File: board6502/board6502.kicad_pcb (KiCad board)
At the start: 2 copper layers, 48 parts, among them J1 IO Pinheader, J2 UART, J3 USB_B, J4 Expansion Port, J5 Power connector, SW1 Reset button, SW2 SW_NMI, U1 DS1813, U2 74LS00, U3 74LS04, U4 W65C22N, U5 74LS30, U6 W65C51N, U7 W65C02, U8 AT28C64B, U9 CY7C199, X1 1-10MHz, Y1 1.8432M

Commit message: start laying out components
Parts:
- J4: footprint Connector_PinHeader_2.54mm:PinHeader_2x17_P2.54mm_Horizontal -> Connector_PinHeader_2.54mm:PinHeader_2x17_P2.54mm_Vertical
- moved C11 277.8 mm to (324.0, 11.0)
- moved U8 239.0 mm to (299.0, 110.5), turned to 270 degrees
- moved J5 188.9 mm to (304.5, 39.0), turned to 90 degrees
- moved SW2 185.9 mm to (249.0, 32.0)
- moved X1 181.9 mm to (265.0, 42.5), turned to 270 degrees
- moved U7 179.1 mm to (260.0, 85.0), turned to 90 degrees
- moved C10 176.5 mm to (250.4, 163.3)
- moved C7 176.5 mm to (287.1, 166.8)
- moved C8 176.5 mm to (259.0, 163.3)
- moved R6 176.5 mm to (295.9, 167.7)
- moved R8 176.5 mm to (299.4, 163.7)
- moved R9 176.5 mm to (278.6, 168.0)
- moved C12 176.5 mm to (299.1, 159.1)
- moved J4 174.5 mm to (302.5, 32.0), turned to 270 degrees
- moved U9 161.7 mm to (293.5, 93.0), turned to 270 degrees
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
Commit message: complete layout
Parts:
- moved R9 124.8 mm to (296.5, 44.5)
- moved D4 121.1 mm to (301.5, 49.0), turned to 270 degrees
- moved R6 116.2 mm to (296.0, 51.5), turned to 90 degrees
- moved C12 114.7 mm to (302.5, 44.5)
- moved R8 112.4 mm to (307.0, 51.5), turned to 90 degrees
- moved C10 110.8 mm to (303.5, 66.0)
- moved C8 103.3 mm to (256.0, 60.0), turned to 270 degrees
- moved C11 94.1 mm to (256.5, 76.5), turned to 90 degrees
- moved C2 93.5 mm to (256.5, 92.5), turned to 270 degrees
- moved C7 53.8 mm to (256.5, 122.5), turned to 270 degrees
- moved R4 43.0 mm to (298.5, 39.5), turned to 180 degrees
- moved J4 42.1 mm to (260.5, 35.0), turned to 90 degrees
- moved C6 5.02 mm to (256.5, 116.5)
- moved C3 1.58 mm to (297.5, 93.0)
- moved U2 1.00 mm to (245.0, 72.0)
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
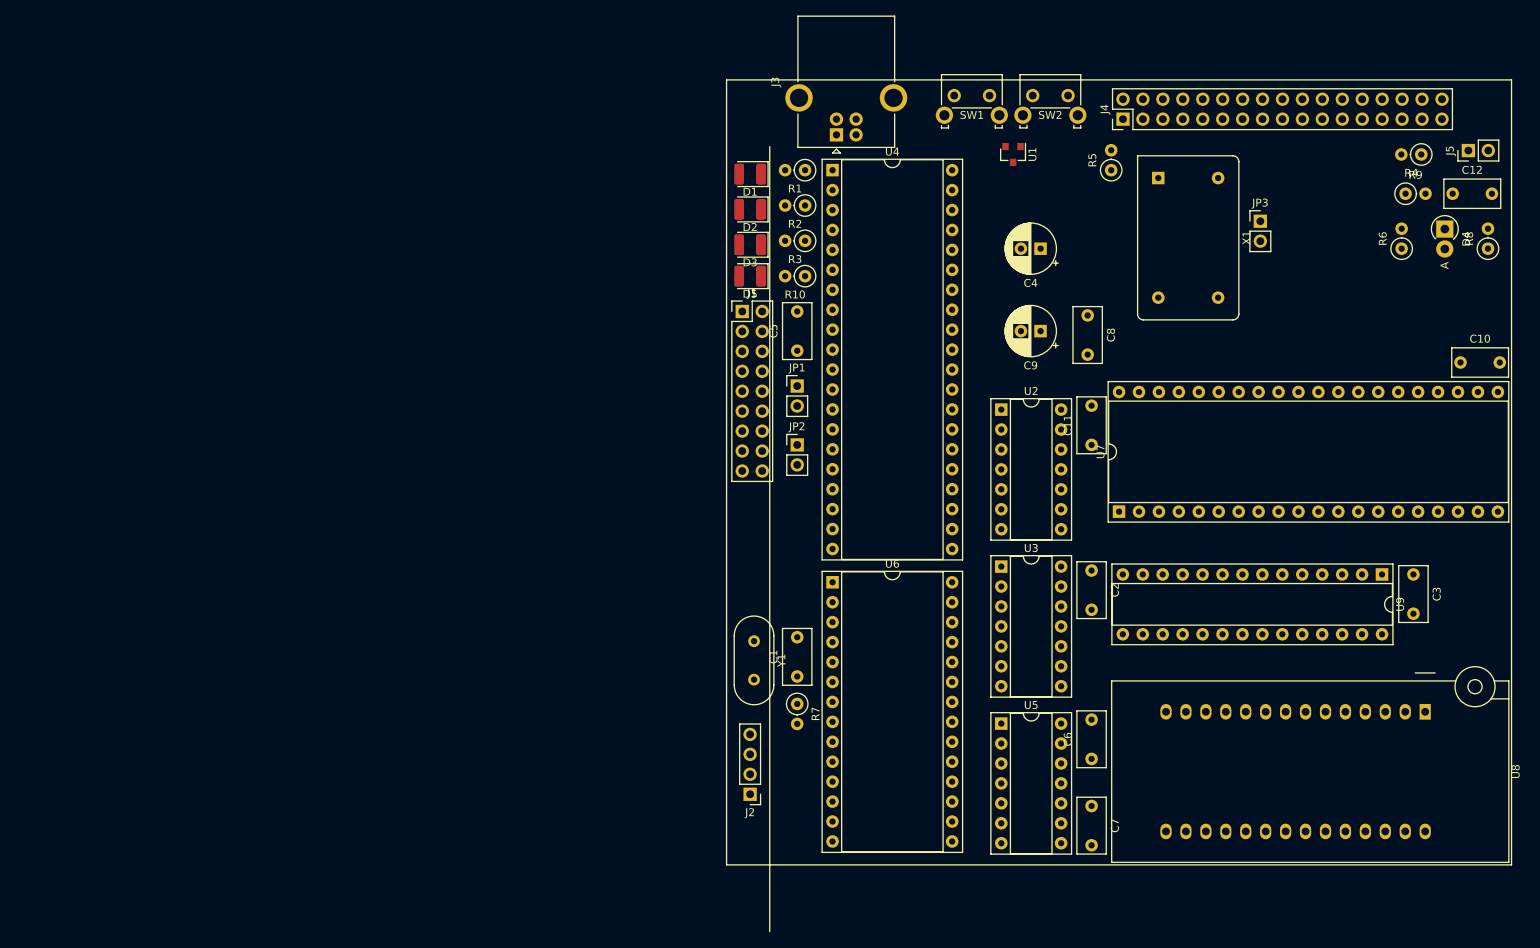
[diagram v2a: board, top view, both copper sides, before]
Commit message: update trace and via sizes
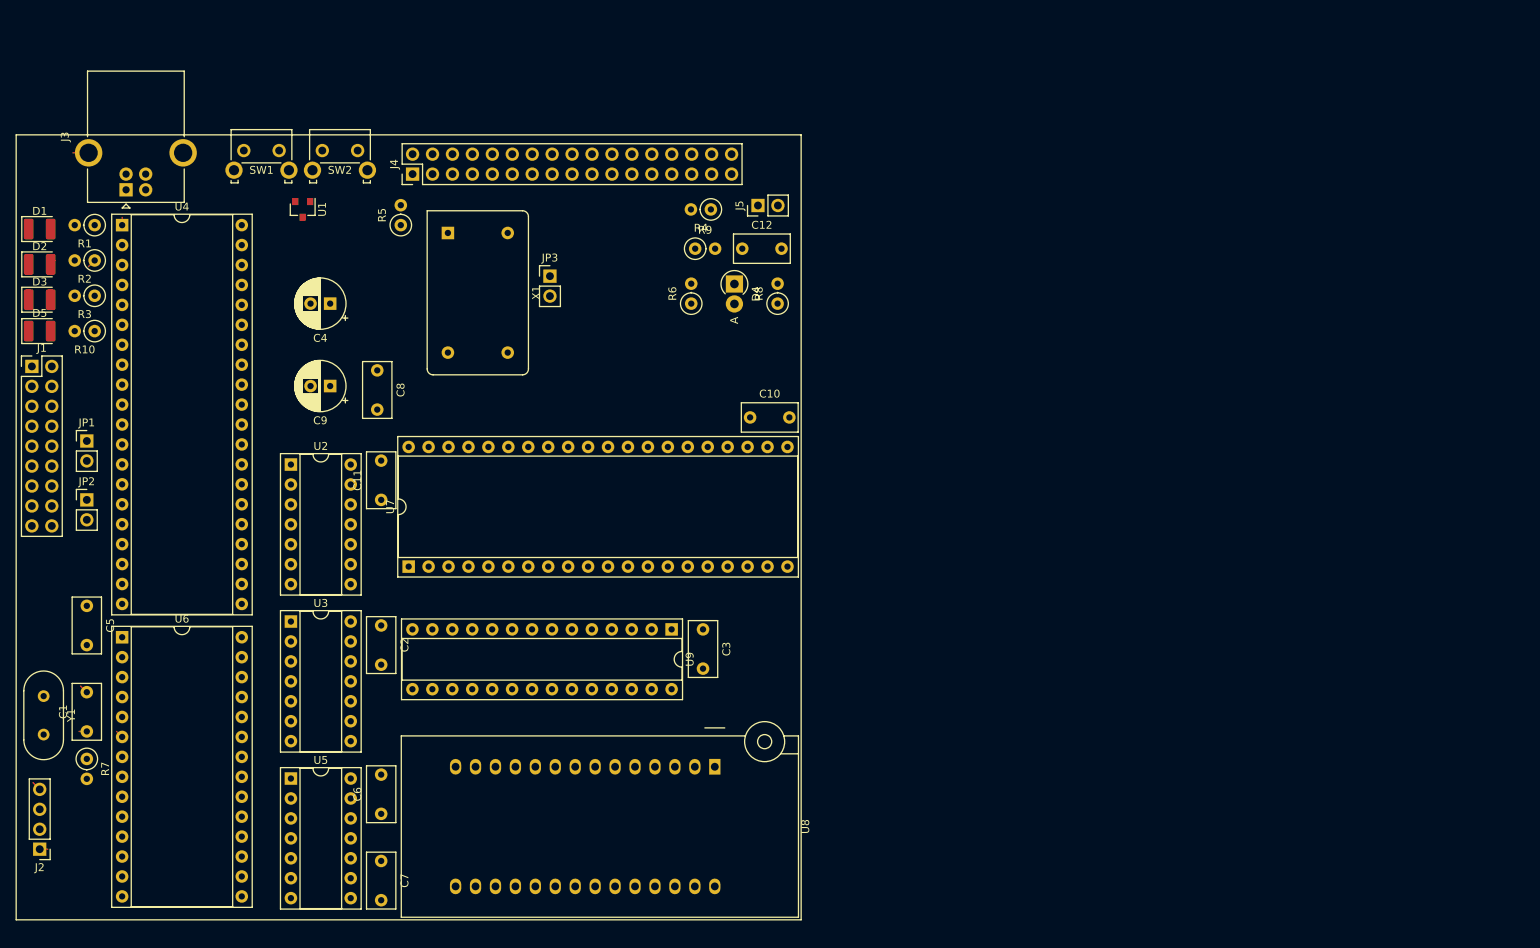
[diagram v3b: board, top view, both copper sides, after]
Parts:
- moved C5 96.2 mm to (128.5, 97.0), turned to 270 degrees
- moved C1 90.8 mm to (128.5, 113.0)
- moved C10 90.8 mm to (213.0, 73.0)
- moved C11 90.8 mm to (166.0, 83.5)
- moved C12 90.8 mm to (212.0, 51.5)
- moved C2 90.8 mm to (166.0, 99.5)
- moved C3 90.8 mm to (207.0, 100.0)
- moved C4 90.8 mm to (159.5, 58.5)
- moved C6 90.8 mm to (166.0, 123.5)
- moved C7 90.8 mm to (166.0, 129.5)
- moved C8 90.8 mm to (165.5, 67.0)
- moved C9 90.8 mm to (159.5, 69.0)
- moved D1 90.8 mm to (122.5, 49.0), turned to 0 degrees
- moved D2 90.8 mm to (122.5, 53.5), turned to 0 degrees
- moved D3 90.8 mm to (122.5, 58.0), turned to 0 degrees
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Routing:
- net GND: track 0.00 -> 6.24 mm
- net +5V: track 0.00 -> 2.07 mm
- net Net-(C1-Pad1): track 0.00 -> 1.99 mm
- net LED1: track 0.00 -> 1.13 mm
- net Net-(D3-Pad2): track 0.00 -> 0.71 mm
- net Net-(D2-Pad2): track 0.00 -> 0.71 mm
- net Net-(D1-Pad2): track 0.00 -> 0.71 mm
- net _SW_RESET: track 0.00 -> 0.62 mm
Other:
- net class Default: clearance 0.2 -> 0.1778; trace_width 0.25 -> 0.1524; via_dia 0.8 -> 0.7; via_drill 0.4 -> 0.35
- net class Power added: clearance 0.1778, trace_width 0.254, via_dia 0.7, via_drill 0.35
- rule trace_clearance: 0.2 -> 0.1778
- rule trace_min: 0.2 -> 0.1524
- rule via_min_drill: 0.3 -> 0.2032
- rule via_min_size: 0.4 -> 0.4572
